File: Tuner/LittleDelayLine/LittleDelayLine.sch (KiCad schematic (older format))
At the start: 115 parts, among them J1 Conn_Coaxial, J10 Conn_Coaxial, J11 Conn_02x05_Odd_Even, J12 Conn_01x01, J13 Conn_01x01, J14 Conn_01x01, J15 Conn_01x01, J16 Conn_01x01, J17 Conn_Coaxial, J18 Conn_01x01, J19 Conn_01x01, J2 Conn_Coaxial, J20 Conn_01x01, J21 Conn_01x01, J22 Conn_Coaxial, J23 Conn_Coaxial, J24 Conn_Coaxial, J25 Conn_01x01, J26 Conn_01x01, J27 Conn_01x01, J28 Conn_01x01, J3 Conn_Coaxial, J4 Conn_Coaxial, J5 Conn_Coaxial, J6 Conn_Coaxial, J7 Conn_Coaxial, J8 Conn_Coaxial, J9 Conn_Coaxial, P10 Conn_01x01, P11 Conn_01x01, P12 Conn_01x01, P2 Conn_01x01, P3 Conn_01x01, P4 Conn_01x01, P5 Conn_01x01, P6 Conn_01x01, P7 Conn_01x01, P8 Conn_01x01, P9 Conn_01x01, U1 MCP23008, U2 ULN2803A

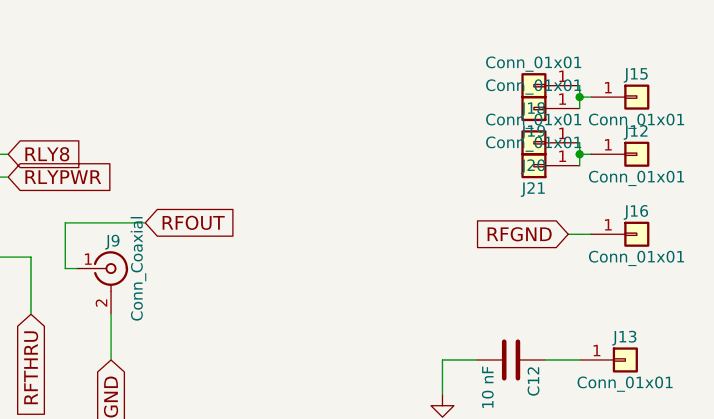
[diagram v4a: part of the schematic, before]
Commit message: Added extra capacitors between relay power and ground posts
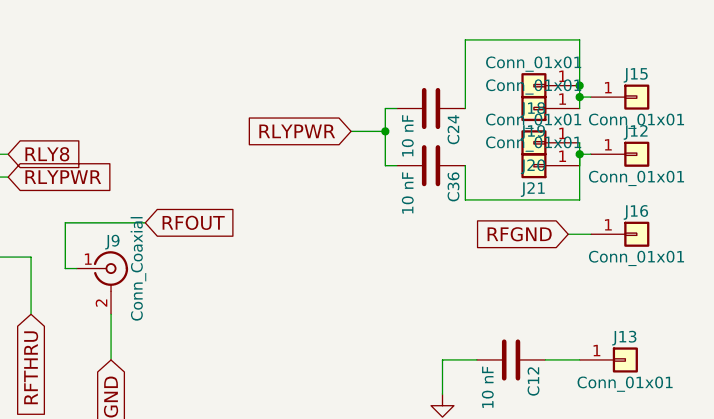
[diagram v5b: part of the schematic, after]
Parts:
- added C24, C36: 10 nF, Capacitors_THT:C_Disc_D5.0mm_W2.5mm_P2.50mm, symbol C
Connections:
- net RLYPWR: now also C24.2, C36.2
- net at J15.1 (Pin_1), J18.1 (Pin_1), J19.1 (Pin_1): now also C24.1
- net at J12.1 (Pin_1), J20.1 (Pin_1), J21.1 (Pin_1): now also C36.1
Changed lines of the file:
@@
 RLY8
 $Comp
-L +5V #PWR12
+L +5V #PWR11
 U 1 1 5B1A0287
 P 3150 5750
-F 0 "#PWR12" H 3150 5600 50  0001 C CNN
+F 0 "#PWR11" H 3150 5600 50  0001 C CNN
 F 1 "+5V" H 3150 5890 50  0000 C CNN
 F 2 "" H 3150 5750 50  0001 C CNN
@@
 $EndComp
 $Comp
-L +5V #PWR9
+L +5V #PWR8
 U 1 1 5B1ABA5A
 P 2150 4450
-F 0 "#PWR9" H 2150 4300 50  0001 C CNN
+F 0 "#PWR8" H 2150 4300 50  0001 C CNN
 F 1 "+5V" H 2150 4590 50  0000 C CNN
 F 2 "" H 2150 4450 50  0001 C CNN
@@
 $EndComp
 $Comp
-L +5V #PWR17
+L +5V #PWR16
 U 1 1 5B1ABFC6
 P 8800 4600
-F 0 "#PWR17" H 8800 4450 50  0001 C CNN
+F 0 "#PWR16" H 8800 4450 50  0001 C CNN
 F 1 "+5V" H 8800 4740 50  0000 C CNN
 F 2 "" H 8800 4600 50  0001 C CNN
@@
 $EndComp
 $Comp
-L GND #PWR18
+L GND #PWR17
 U 1 1 5B1AC04C
 P 8800 5150
-F 0 "#PWR18" H 8800 4900 50  0001 C CNN
+F 0 "#PWR17" H 8800 4900 50  0001 C CNN
 F 1 "GND" H 8800 5000 50  0000 C CNN
 F 2 "" H 8800 5150 50  0001 C CNN
@@
 $EndComp
 $Comp
-L GND #PWR15
+L GND #PWR14
 U 1 1 5B9A4AE1
 P 4850 6650
-F 0 "#PWR15" H 4850 6400 50  0001 C CNN
+F 0 "#PWR14" H 4850 6400 50  0001 C CNN
 F 1 "GND" H 4850 6500 50  0000 C CNN
 F 2 "" H 4850 6650 50  0001 C CNN
@@
 $EndComp
 $Comp
-L GND #PWR14
+L GND #PWR13
 U 1 1 5B9ACA36
 P 3550 6100
-F 0 "#PWR14" H 3550 5850 50  0001 C CNN
+F 0 "#PWR13" H 3550 5850 50  0001 C CNN
 F 1 "GND" H 3550 5950 50  0000 C CNN
 F 2 "" H 3550 6100 50  0001 C CNN
@@
 $EndComp
 $Comp
-L GND #PWR16
+L GND #PWR15
 U 1 1 5BAEE216
 P 5050 7250
-F 0 "#PWR16" H 5050 7000 50  0001 C CNN
+F 0 "#PWR15" H 5050 7000 50  0001 C CNN
 F 1 "GND" H 5050 7100 50  0000 C CNN
 F 2 "" H 5050 7250 50  0001 C CNN
@@
 Text GLabel 8800 1900 3    60   Input ~ 0
 RFGND
+Text GLabel 8950 1300 2    60   Input ~ 0
+RFOUT
+$Comp
+L R R1
+U 1 1 5C758092
+P 2250 4200
+F 0 "R1" V 2330 4200 50  0000 C CNN
+F 1 "10k" V 2250 4200 50  0000 C CNN
+F 2 "Resistors_THT:R_Axial_DIN0207_L6.3mm_D2.5mm_P7.62mm_Horizontal" V 2180 4200 50  0001 C CNN
+F 3 "" H 2250 4200 50  0001 C CNN
+	1    2250 4200
+	1    0    0    -1
+$EndComp
+$Comp
+L R R2
+U 1 1 5C758466
+P 2400 4200
+F 0 "R2" V 2480 4200 50  0000 C CNN
+F 1 "10k" V 2400 4200 50  0000 C CNN
+F 2 "Resistors_THT:R_Axial_DIN0207_L6.3mm_D2.5mm_P7.62mm_Horizontal" V 2330 4200 50  0001 C CNN
+F 3 "" H 2400 4200 50  0001 C CNN
+	1    2400 4200
+	1    0    0    -1
+$EndComp
+$Comp
+L +5V #PWR9
+U 1 1 5C7585CE
+P 2250 4000
+F 0 "#PWR9" H 2250 3850 50  0001 C CNN
+F 1 "+5V" H 2250 4140 50  0000 C CNN
+F 2 "" H 2250 4000 50  0001 C CNN
+F 3 "" H 2250 4000 50  0001 C CNN
+	1    2250 4000
+	1    0    0    -1
+$EndComp
+$Comp
+L +5V #PWR10
+U 1 1 5C7589BF
+P 2400 4000
+F 0 "#PWR10" H 2400 3850 50  0001 C CNN
+F 1 "+5V" H 2400 4140 50  0000 C CNN
+F 2 "" H 2400 4000 50  0001 C CNN
+F 3 "" H 2400 4000 50  0001 C CNN
+	1    2400 4000
+	1    0    0    -1
+$EndComp
+$Comp
+L GND #PWR12
+U 1 1 5C758F92
+P 3300 4250
+F 0 "#PWR12" H 3300 4000 50  0001 C CNN
+F 1 "GND" H 3300 4100 50  0000 C CNN
+F 2 "" H 3300 4250 50  0001 C CNN
+F 3 "" H 3300 4250 50  0001 C CNN
+	1    3300 4250
+	1    0    0    -1
+$EndComp
+$Comp
+L Conn_01x01 J28
+U 1 1 5C745726
+P 7950 2200
+F 0 "J28" H 7950 2300 50  0000 C CNN
+F 1 "Conn_01x01" H 7950 2100 50  0000 C CNN
+F 2 "Connectors:1pin" H 7950 2200 50  0001 C CNN
+F 3 "" H 7950 2200 50  0001 C CNN
+	1    7950 2200
+	0    1    1    0
+$EndComp
+$Comp
+L Conn_Coaxial J8
+U 1 1 5C7C04B6
+P 700 2750
+F 0 "J8" H 710 2870 50  0000 C CNN
+F 1 "Conn_Coaxial" V 815 2750 50  0000 C CNN
+F 2 "tuner:bnc_90_1-1337543-0_pad_combo" H 700 2750 50  0001 C CNN
+F 3 "" H 700 2750 50  0001 C CNN
+	1    700  2750
+	-1   0    0    -1
+$EndComp
+$Comp
+L Conn_Coaxial J9
+U 1 1 5C7C0EBB
+P 8800 1500
+F 0 "J9" H 8810 1620 50  0000 C CNN
+F 1 "Conn_Coaxial" V 8915 1500 50  0000 C CNN
+F 2 "tuner:bnc_90_1-1337543-0_pad_combo" H 8800 1500 50  0001 C CNN
+F 3 "" H 8800 1500 50  0001 C CNN
+	1    8800 1500
+	1    0    0    -1
+$EndComp
+Text GLabel 8450 1700 3    60   Input ~ 0
+RFTHRU
+$Comp
+L DPDTRelay RLY1
+U 1 1 5C74004F
+P 1700 3150
+F 0 "RLY1" H 1950 3000 60  0000 C CNN
+F 1 "DPDTRelay" H 1400 3450 60  0000 C CNN
+F 2 "tuner:G2VRelay" H 1700 3150 60  0001 C CNN
+F 3 "" H 1700 3150 60  0001 C CNN
+	1    1700 3150
+	1    0    0    -1
+$EndComp
+Text GLabel 2500 2800 2    60   Input ~ 0
+RFTHRU
 Connection ~ 9650 5350
 Wire Wire Line
@@
 	10900 1350 10800 1350
 Wire Wire Line
-	10850 700  10850 800
+	10850 500  10850 800
 Wire Wire Line
 	10850 750  10900 750
@@
 Wire Wire Line
 	7750 1850 7750 2000
-Text GLabel 8950 1300 2    60   Input ~ 0
-RFOUT
 Wire Wire Line
 	8950 1300 8600 1300
-$Comp
-L R R1
-U 1 1 5C758092
-P 2250 4200
-F 0 "R1" V 2330 4200 50  0000 C CNN
-F 1 "10k" V 2250 4200 50  0000 C CNN
-F 2 "Resistors_THT:R_Axial_DIN0207_L6.3mm_D2.5mm_P7.62mm_Horizontal" V 2180 4200 50  0001 C CNN
-F 3 "" H 2250 4200 50  0001 C CNN
-	1    2250 4200
-	1    0    0    -1
-$EndComp
-$Comp
-L R R2
-U 1 1 5C758466
-P 2400 4200
-F 0 "R2" V 2480 4200 50  0000 C CNN
-F 1 "10k" V 2400 4200 50  0000 C CNN
-F 2 "Resistors_THT:R_Axial_DIN0207_L6.3mm_D2.5mm_P7.62mm_Horizontal" V 2330 4200 50  0001 C CNN
-F 3 "" H 2400 4200 50  0001 C CNN
-	1    2400 4200
-	1    0    0    -1
-$EndComp
-$Comp
-L +5V #PWR10
-U 1 1 5C7585CE
-P 2250 4000
-F 0 "#PWR10" H 2250 3850 50  0001 C CNN
-F 1 "+5V" H 2250 4140 50  0000 C CNN
-F 2 "" H 2250 4000 50  0001 C CNN
-F 3 "" H 2250 4000 50  0001 C CNN
-	1    2250 4000
-	1    0    0    -1
-$EndComp
 Wire Wire Line
 	2250 4000 2250 4050
-$Comp
-L +5V #PWR11
-U 1 1 5C7589BF
-P 2400 4000
-F 0 "#PWR11" H 2400 3850 50  0001 C CNN
-F 1 "+5V" H 2400 4140 50  0000 C CNN
-F 2 "" H 2400 4000 50  0001 C CNN
-F 3 "" H 2400 4000 50  0001 C CNN
-	1    2400 4000
-	1    0    0    -1
-$EndComp
 Wire Wire Line
 	2400 4000 2400 4050
-$Comp
-L GND #PWR13
-U 1 1 5C758F92
-P 3300 4250
-F 0 "#PWR13" H 3300 4000 50  0001 C CNN
-F 1 "GND" H 3300 4100 50  0000 C CNN
-F 2 "" H 3300 4250 50  0001 C CNN
-F 3 "" H 3300 4250 50  0001 C CNN
-	1    3300 4250
-	1    0    0    -1
-$EndComp
 Wire Wire Line
 	3300 4200 3300 4300
@@
 	3150 4200 3300 4200
 Connection ~ 3300 4250
-$Comp
-L Conn_01x01 J28
-U 1 1 5C745726
-P 7950 2200
-F 0 "J28" H 7950 2300 50  0000 C CNN
-F 1 "Conn_01x01" H 7950 2100 50  0000 C CNN
-F 2 "Connectors:1pin" H 7950 2200 50  0001 C CNN
-F 3 "" H 7950 2200 50  0001 C CNN
-	1    7950 2200
-	0    1    1    0
-$EndComp
 Wire Wire Line
 	7950 2000 7950 1950
@@
 	7950 1950 7750 1950
 Connection ~ 7750 1950
-$Comp
-L Conn_Coaxial J8
-U 1 1 5C7C04B6
-P 700 2750
-F 0 "J8" H 710 2870 50  0000 C CNN
-F 1 "Conn_Coaxial" V 815 2750 50  0000 C CNN
-F 2 "tuner:bnc_90_1-1337543-0_pad_combo" H 700 2750 50  0001 C CNN
-F 3 "" H 700 2750 50  0001 C CNN
-	1    700  2750
-	-1   0    0    -1
-$EndComp
 Wire Wire Line
 	1000 2950 700  2950
-$Comp
-L Conn_Coaxial J9
-U 1 1 5C7C0EBB
-P 8800 1500
-F 0 "J9" H 8810 1620 50  0000 C CNN
-F 1 "Conn_Coaxial" V 8915 1500 50  0000 C CNN
-F 2 "tuner:bnc_90_1-1337543-0_pad_combo" H 8800 1500 50  0001 C CNN
-F 3 "" H 8800 1500 50  0001 C CNN
-	1    8800 1500
-	1    0    0    -1
-$EndComp
 Wire Wire Line
 	2250 3400 2250 3450
@@
 Wire Wire Line
 	8800 1700 8800 1900
-Text GLabel 8450 1700 3    60   Input ~ 0
-RFTHRU
 Wire Wire Line
 	8450 1700 8450 1450
@@
 	8450 1450 8250 1450
 Connection ~ 8250 1450
-$Comp
-L DPDTRelay RLY1
-U 1 1 5C74004F
-P 1700 3150
-F 0 "RLY1" H 1950 3000 60  0000 C CNN
-F 1 "DPDTRelay" H 1400 3450 60  0000 C CNN
-F 2 "tuner:G2VRelay" H 1700 3150 60  0001 C CNN
-F 3 "" H 1700 3150 60  0001 C CNN
-	1    1700 3150
-	1    0    0    -1
-$EndComp
 Wire Wire Line
 	1150 3050 1050 3050
@@
 Wire Wire Line
 	1100 2700 1150 2700
-Text GLabel 2500 2800 2    60   Input ~ 0
-RFTHRU
 Wire Wire Line
 	2500 2800 2200 2800
@@
 	1850 5200 1850 5300
 Connection ~ 850  5500
+$Comp
+L C C24
+U 1 1 5DDB910C
+P 10200 800
+F 0 "C24" H 10225 900 50  0000 L CNN
+F 1 "10 nF" H 10225 700 50  0000 L CNN
+F 2 "Capacitors_THT:C_Disc_D5.0mm_W2.5mm_P2.50mm" H 10238 650 50  0001 C CNN
+F 3 "" H 10200 800 50  0001 C CNN
+	1    10200 800
+	0    1    1    0
+$EndComp
+Wire Wire Line
+	10050 800  10000 800
+$Comp
+L C C36
+U 1 1 5DDB9595
+P 10200 1050
+F 0 "C36" H 10225 1150 50  0000 L CNN
+F 1 "10 nF" H 10225 950 50  0000 L CNN
+F 2 "Capacitors_THT:C_Disc_D5.0mm_W2.5mm_P2.50mm" H 10238 900 50  0001 C CNN
+F 3 "" H 10200 1050 50  0001 C CNN
+	1    10200 1050
+	0    1    1    0
+$EndComp
+Wire Wire Line
+	10000 800  10000 1050
+Wire Wire Line
+	10000 1050 10050 1050
+Wire Wire Line
+	10350 800  10350 500
+Wire Wire Line
+	10350 500  10850 500
+Connection ~ 10850 700
+Wire Wire Line
+	10850 1000 10850 1200
+Wire Wire Line
+	10850 1200 10350 1200
+Wire Wire Line
+	10350 1200 10350 1050
+Text GLabel 9850 900  0    60   Input ~ 0
+RLYPWR
+Wire Wire Line
+	9850 900  10000 900
+Connection ~ 10000 900
 $EndSCHEMATC

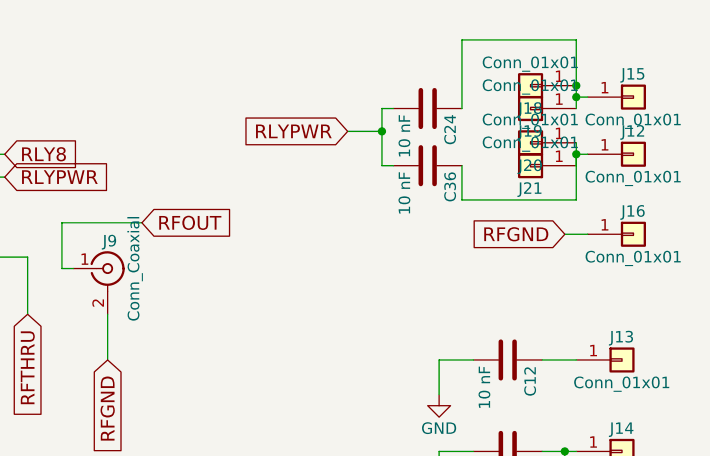
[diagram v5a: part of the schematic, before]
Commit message: Changed some of the capacitors to NC becaue they might cause problems in some situations
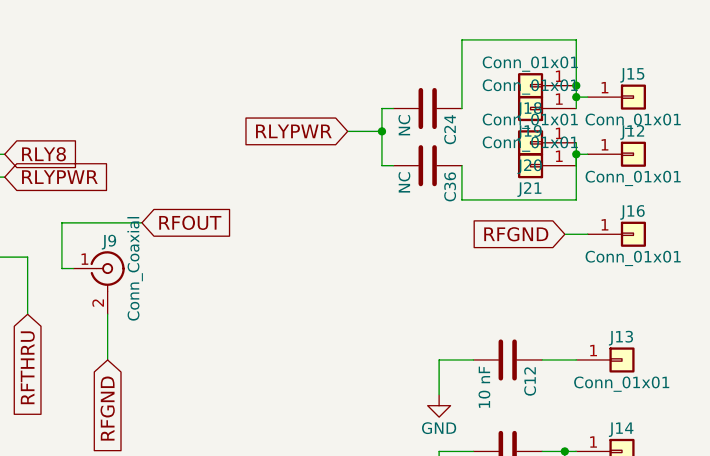
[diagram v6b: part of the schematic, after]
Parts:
- C24, C36: value 10 nF -> NC
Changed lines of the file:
@@
 P 10200 800
 F 0 "C24" H 10225 900 50  0000 L CNN
-F 1 "10 nF" H 10225 700 50  0000 L CNN
+F 1 "NC" H 10225 700 50  0000 L CNN
 F 2 "Capacitors_THT:C_Disc_D5.0mm_W2.5mm_P2.50mm" H 10238 650 50  0001 C CNN
 F 3 "" H 10200 800 50  0001 C CNN
@@
 P 10200 1050
 F 0 "C36" H 10225 1150 50  0000 L CNN
-F 1 "10 nF" H 10225 950 50  0000 L CNN
+F 1 "NC" H 10225 950 50  0000 L CNN
 F 2 "Capacitors_THT:C_Disc_D5.0mm_W2.5mm_P2.50mm" H 10238 900 50  0001 C CNN
 F 3 "" H 10200 1050 50  0001 C CNN

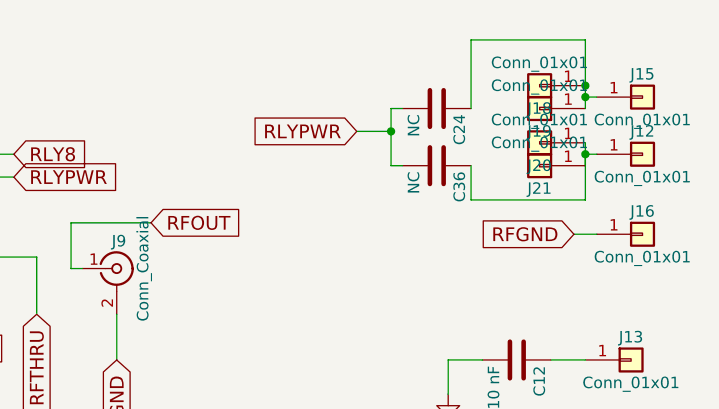
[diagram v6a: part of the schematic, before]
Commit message: Added extra mounting holes to ground ReversibleLittleSection
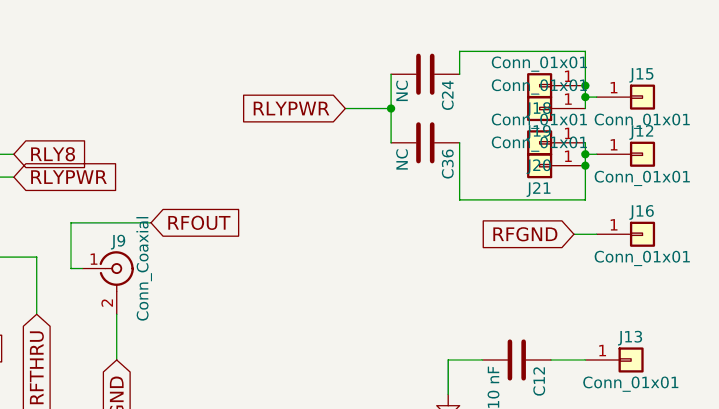
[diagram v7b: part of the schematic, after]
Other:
- moved on the sheet: C24, C36
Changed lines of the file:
@@
 RLY8
 $Comp
-L +5V #PWR11
+L +5V #PWR01
 U 1 1 5B1A0287
 P 3150 5750
-F 0 "#PWR11" H 3150 5600 50  0001 C CNN
+F 0 "#PWR01" H 3150 5600 50  0001 C CNN
 F 1 "+5V" H 3150 5890 50  0000 C CNN
 F 2 "" H 3150 5750 50  0001 C CNN
@@
 $EndComp
 $Comp
-L GND #PWR3
+L GND #PWR02
 U 1 1 5B1AA0F6
 P 900 4500
-F 0 "#PWR3" H 900 4250 50  0001 C CNN
+F 0 "#PWR02" H 900 4250 50  0001 C CNN
 F 1 "GND" H 900 4350 50  0000 C CNN
 F 2 "" H 900 4500 50  0001 C CNN
@@
 $EndComp
 $Comp
-L +5V #PWR2
+L +5V #PWR03
 U 1 1 5B1AABE9
 P 900 3750
-F 0 "#PWR2" H 900 3600 50  0001 C CNN
+F 0 "#PWR03" H 900 3600 50  0001 C CNN
 F 1 "+5V" H 900 3890 50  0000 C CNN
 F 2 "" H 900 3750 50  0001 C CNN
@@
 $EndComp
 $Comp
-L +5V #PWR8
+L +5V #PWR04
 U 1 1 5B1ABA5A
 P 2150 4450
-F 0 "#PWR8" H 2150 4300 50  0001 C CNN
+F 0 "#PWR04" H 2150 4300 50  0001 C CNN
 F 1 "+5V" H 2150 4590 50  0000 C CNN
 F 2 "" H 2150 4450 50  0001 C CNN
@@
 $EndComp
 $Comp
-L +5V #PWR16
+L +5V #PWR05
 U 1 1 5B1ABFC6
 P 8800 4600
-F 0 "#PWR16" H 8800 4450 50  0001 C CNN
+F 0 "#PWR05" H 8800 4450 50  0001 C CNN
 F 1 "+5V" H 8800 4740 50  0000 C CNN
 F 2 "" H 8800 4600 50  0001 C CNN
@@
 $EndComp
 $Comp
-L GND #PWR17
+L GND #PWR06
 U 1 1 5B1AC04C
 P 8800 5150
-F 0 "#PWR17" H 8800 4900 50  0001 C CNN
+F 0 "#PWR06" H 8800 4900 50  0001 C CNN
 F 1 "GND" H 8800 5000 50  0000 C CNN
 F 2 "" H 8800 5150 50  0001 C CNN
@@
 $EndComp
 $Comp
-L GND #PWR14
+L GND #PWR07
 U 1 1 5B9A4AE1
 P 4850 6650
-F 0 "#PWR14" H 4850 6400 50  0001 C CNN
+F 0 "#PWR07" H 4850 6400 50  0001 C CNN
 F 1 "GND" H 4850 6500 50  0000 C CNN
 F 2 "" H 4850 6650 50  0001 C CNN
@@
 $EndComp
 $Comp
-L GND #PWR13
+L GND #PWR08
 U 1 1 5B9ACA36
 P 3550 6100
-F 0 "#PWR13" H 3550 5850 50  0001 C CNN
+F 0 "#PWR08" H 3550 5850 50  0001 C CNN
 F 1 "GND" H 3550 5950 50  0000 C CNN
 F 2 "" H 3550 6100 50  0001 C CNN
@@
 $EndComp
 $Comp
-L GND #PWR19
+L GND #PWR09
 U 1 1 5B982525
 P 10250 2050
-F 0 "#PWR19" H 10250 1800 50  0001 C CNN
+F 0 "#PWR09" H 10250 1800 50  0001 C CNN
 F 1 "GND" H 10250 1900 50  0000 C CNN
 F 2 "" H 10250 2050 50  0001 C CNN
@@
 $EndComp
 $Comp
-L GND #PWR7
+L GND #PWR010
 U 1 1 5BA4D8F3
 P 1800 5850
-F 0 "#PWR7" H 1800 5600 50  0001 C CNN
+F 0 "#PWR010" H 1800 5600 50  0001 C CNN
 F 1 "GND" H 1800 5700 50  0000 C CNN
 F 2 "" H 1800 5850 50  0001 C CNN
@@
 $EndComp
 $Comp
-L +5V #PWR6
+L +5V #PWR011
 U 1 1 5BA4E663
 P 1200 5700
-F 0 "#PWR6" H 1200 5550 50  0001 C CNN
+F 0 "#PWR011" H 1200 5550 50  0001 C CNN
 F 1 "+5V" H 1200 5840 50  0000 C CNN
 F 2 "" H 1200 5700 50  0001 C CNN
@@
 $EndComp
 $Comp
-L GND #PWR1
+L GND #PWR012
 U 1 1 5BA4FB25
 P 750 5900
-F 0 "#PWR1" H 750 5650 50  0001 C CNN
+F 0 "#PWR012" H 750 5650 50  0001 C CNN
 F 1 "GND" H 750 5750 50  0000 C CNN
 F 2 "" H 750 5900 50  0001 C CNN
@@
 $EndComp
 $Comp
-L GND #PWR5
+L GND #PWR013
 U 1 1 5BA5005D
 P 1100 5300
-F 0 "#PWR5" H 1100 5050 50  0001 C CNN
+F 0 "#PWR013" H 1100 5050 50  0001 C CNN
 F 1 "GND" H 1100 5150 50  0000 C CNN
 F 2 "" H 1100 5300 50  0001 C CNN
@@
 EXTPWR
 $Comp
-L +5V #PWR4
+L +5V #PWR014
 U 1 1 5BAE4DBC
 P 1000 4850
-F 0 "#PWR4" H 1000 4700 50  0001 C CNN
+F 0 "#PWR014" H 1000 4700 50  0001 C CNN
 F 1 "+5V" H 1000 4990 50  0000 C CNN
 F 2 "" H 1000 4850 50  0001 C CNN
@@
 $EndComp
 $Comp
-L GND #PWR15
+L GND #PWR015
 U 1 1 5BAEE216
 P 5050 7250
-F 0 "#PWR15" H 5050 7000 50  0001 C CNN
+F 0 "#PWR015" H 5050 7000 50  0001 C CNN
 F 1 "GND" H 5050 7100 50  0000 C CNN
 F 2 "" H 5050 7250 50  0001 C CNN
@@
 $EndComp
 $Comp
-L +5V #PWR9
+L +5V #PWR016
 U 1 1 5C7585CE
 P 2250 4000
-F 0 "#PWR9" H 2250 3850 50  0001 C CNN
+F 0 "#PWR016" H 2250 3850 50  0001 C CNN
 F 1 "+5V" H 2250 4140 50  0000 C CNN
 F 2 "" H 2250 4000 50  0001 C CNN
@@
 $EndComp
 $Comp
-L +5V #PWR10
+L +5V #PWR017
 U 1 1 5C7589BF
 P 2400 4000
-F 0 "#PWR10" H 2400 3850 50  0001 C CNN
+F 0 "#PWR017" H 2400 3850 50  0001 C CNN
 F 1 "+5V" H 2400 4140 50  0000 C CNN
 F 2 "" H 2400 4000 50  0001 C CNN
@@
 $EndComp
 $Comp
-L GND #PWR12
+L GND #PWR018
 U 1 1 5C758F92
 P 3300 4250
-F 0 "#PWR12" H 3300 4000 50  0001 C CNN
+F 0 "#PWR018" H 3300 4000 50  0001 C CNN
 F 1 "GND" H 3300 4100 50  0000 C CNN
 F 2 "" H 3300 4250 50  0001 C CNN
@@
 	10900 1350 10800 1350
 Wire Wire Line
-	10850 500  10850 800
+	10850 550  10850 800
 Wire Wire Line
 	10850 750  10900 750
 Connection ~ 10850 750
 Wire Wire Line
-	10850 950  10850 1050
+	10850 950  10850 1200
 Wire Wire Line
 	10850 1000 10900 1000
@@
 L C C24
 U 1 1 5DDB910C
-P 10200 800
-F 0 "C24" H 10225 900 50  0000 L CNN
-F 1 "NC" H 10225 700 50  0000 L CNN
-F 2 "Capacitors_THT:C_Disc_D5.0mm_W2.5mm_P2.50mm" H 10238 650 50  0001 C CNN
-F 3 "" H 10200 800 50  0001 C CNN
-	1    10200 800
-	0    1    1    0
-$EndComp
-Wire Wire Line
-	10050 800  10000 800
+P 10150 650
+F 0 "C24" H 10175 750 50  0000 L CNN
+F 1 "NC" H 10175 550 50  0000 L CNN
+F 2 "Capacitors_THT:C_Disc_D5.0mm_W2.5mm_P2.50mm" H 10188 500 50  0001 C CNN
+F 3 "" H 10150 650 50  0001 C CNN
+	1    10150 650
+	0    1    1    0
+$EndComp
 $Comp
 L C C36
 U 1 1 5DDB9595
-P 10200 1050
-F 0 "C36" H 10225 1150 50  0000 L CNN
-F 1 "NC" H 10225 950 50  0000 L CNN
-F 2 "Capacitors_THT:C_Disc_D5.0mm_W2.5mm_P2.50mm" H 10238 900 50  0001 C CNN
-F 3 "" H 10200 1050 50  0001 C CNN
-	1    10200 1050
-	0    1    1    0
-$EndComp
-Wire Wire Line
-	10000 800  10000 1050
-Wire Wire Line
-	10000 1050 10050 1050
-Wire Wire Line
-	10350 800  10350 500
-Wire Wire Line
-	10350 500  10850 500
+P 10150 950
+F 0 "C36" H 10175 1050 50  0000 L CNN
+F 1 "NC" H 10175 850 50  0000 L CNN
+F 2 "Capacitors_THT:C_Disc_D5.0mm_W2.5mm_P2.50mm" H 10188 800 50  0001 C CNN
+F 3 "" H 10150 950 50  0001 C CNN
+	1    10150 950
+	0    1    1    0
+$EndComp
+Text GLabel 9800 800  0    60   Input ~ 0
+RLYPWR
+Wire Wire Line
+	9800 800  10000 800
+Wire Wire Line
+	10000 650  10000 950
+Connection ~ 10000 800
+Wire Wire Line
+	10300 550  10300 650
+Wire Wire Line
+	10300 950  10300 1200
+Wire Wire Line
+	10300 550  10850 550
 Connection ~ 10850 700
 Wire Wire Line
-	10850 1000 10850 1200
-Wire Wire Line
-	10850 1200 10350 1200
-Wire Wire Line
-	10350 1200 10350 1050
-Text GLabel 9850 900  0    60   Input ~ 0
-RLYPWR
-Wire Wire Line
-	9850 900  10000 900
-Connection ~ 10000 900
+	10300 1200 10850 1200
+Connection ~ 10850 1050
 $EndSCHEMATC
